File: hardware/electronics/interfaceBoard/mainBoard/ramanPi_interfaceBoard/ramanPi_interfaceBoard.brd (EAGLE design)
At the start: 151.1 x 89.8 mm, 11 parts

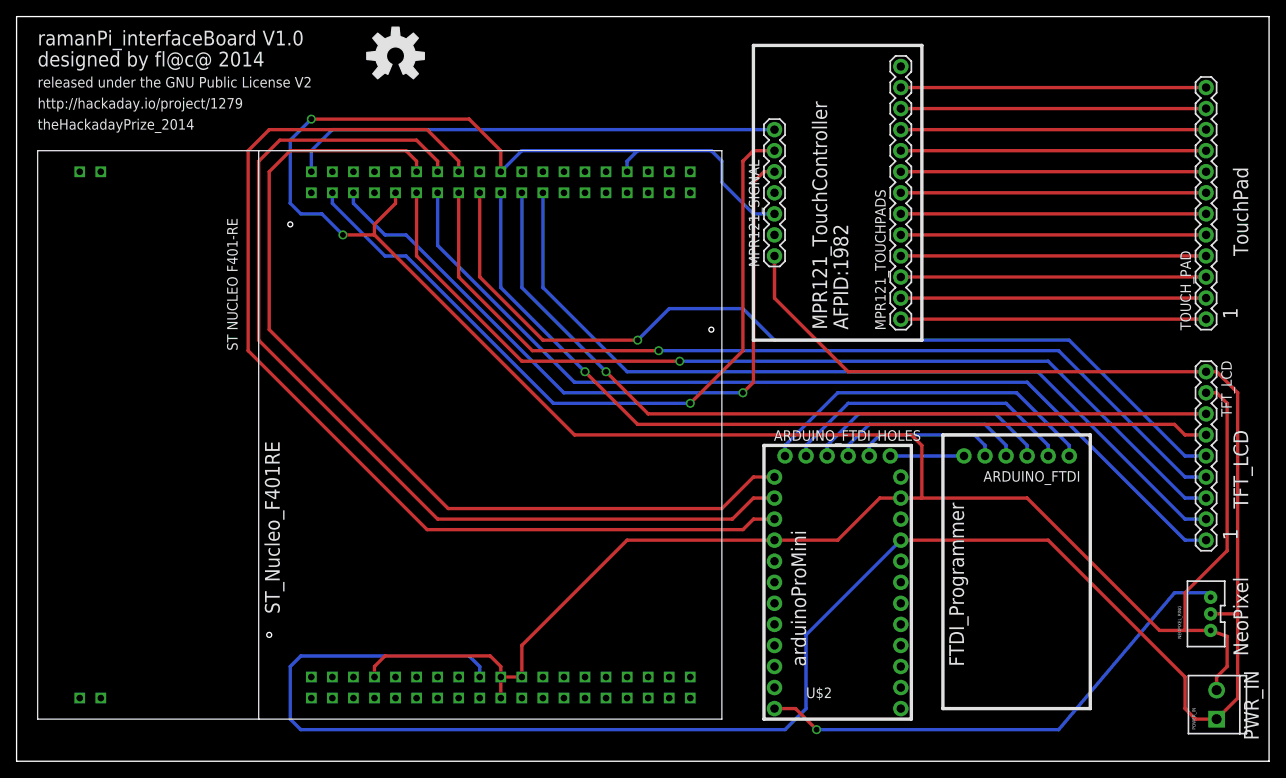
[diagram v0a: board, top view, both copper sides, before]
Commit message: updated Nucleo library in all board layouts
Updated Nucleo F401_RE library for better drill hole sizes
updated all boards to include new library changes
---need to update all studio files, svg, etc..
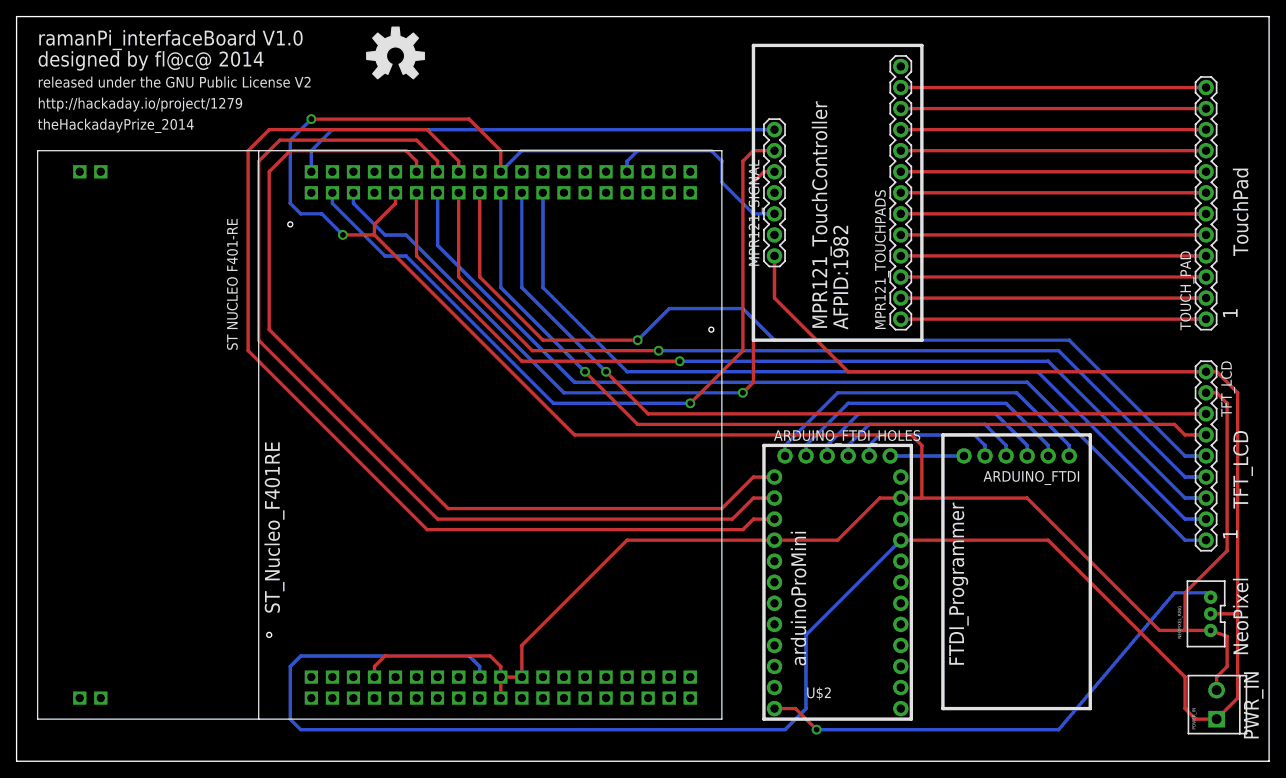
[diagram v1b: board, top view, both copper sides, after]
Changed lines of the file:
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@@
 </classes>
 <designrules>
-<description language="de">&lt;b&gt;EAGLE Design Rules&lt;/b&gt;
-&lt;p&gt;
-Die Standard-Design-Rules sind so gewählt, dass sie für
-die meisten Anwendungen passen. Sollte ihre Platine
-besondere Anforderungen haben, treffen Sie die erforderlichen
-Einstellungen hier und speichern die Design Rules unter
-einem neuen Namen ab.</description>
 <description language="en">&lt;b&gt;EAGLE Design Rules&lt;/b&gt;
 &lt;p&gt;
@@
 <param name="mdViaViaSameLayer" value="8mil"/>
 <param name="mnLayersViaInSmd" value="2"/>
-<param name="mdCopperDimension" value="40mil"/>
+<param name="mdCopperDimension" value="10mil"/>
 <param name="mdDrill" value="8mil"/>
 <param name="mdSmdStop" value="0mil"/>
-<param name="msWidth" value="10mil"/>
-<param name="msDrill" value="24mil"/>
+<param name="msWidth" value="8mil"/>
+<param name="msDrill" value="20mil"/>
 <param name="msMicroVia" value="9.99mm"/>
 <param name="msBlindViaRatio" value="0.5"/>
@@
 <param name="rvMicroViaOuter" value="0.25"/>
 <param name="rvMicroViaInner" value="0.25"/>
-<param name="rlMinPadTop" value="10mil"/>
+<param name="rlMinPadTop" value="12mil"/>
 <param name="rlMaxPadTop" value="20mil"/>
 <param name="rlMinPadInner" value="10mil"/>
 <param name="rlMaxPadInner" value="20mil"/>
-<param name="rlMinPadBottom" value="10mil"/>
+<param name="rlMinPadBottom" value="12mil"/>
 <param name="rlMaxPadBottom" value="20mil"/>
-<param name="rlMinViaOuter" value="8mil"/>
+<param name="rlMinViaOuter" value="10mil"/>
 <param name="rlMaxViaOuter" value="20mil"/>
-<param name="rlMinViaInner" value="8mil"/>
+<param name="rlMinViaInner" value="10mil"/>
 <param name="rlMaxViaInner" value="20mil"/>
 <param name="rlMinMicroViaOuter" value="4mil"/>
@@
 <param name="mlMinCreamFrame" value="0mil"/>
 <param name="mlMaxCreamFrame" value="0mil"/>
-<param name="mlViaStopLimit" value="0mil"/>
+<param name="mlViaStopLimit" value="25mil"/>
 <param name="srRoundness" value="0"/>
 <param name="srMinRoundness" value="0mil"/>

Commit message: update
updated all boards and schematics
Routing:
- net N$25: track 347.2 -> 346.4 mm
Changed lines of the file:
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@@
 <wire x1="146.05" y1="25.4" x2="140.97" y2="20.32" width="0.4064" layer="1"/>
 <wire x1="140.97" y1="20.32" x2="140.97" y2="15.78" width="0.4064" layer="1"/>
-<wire x1="144.78" y1="8.58" x2="144.78" y2="10.16" width="0.4064" layer="1"/>
-<wire x1="144.78" y1="10.16" x2="146.05" y2="11.43" width="0.4064" layer="1"/>
-<wire x1="146.05" y1="11.43" x2="146.05" y2="15.06" width="0.4064" layer="1"/>
-<wire x1="146.05" y1="15.06" x2="144.06" y2="15.78" width="0.4064" layer="1"/>
+<wire x1="144.78" y1="8.58" x2="144.78" y2="15.06" width="0.4064" layer="1"/>
+<wire x1="144.78" y1="15.06" x2="144.06" y2="15.78" width="0.4064" layer="1"/>
 <wire x1="106.68" y1="31.75" x2="104.14" y2="31.75" width="0.4064" layer="1"/>
 <wire x1="104.14" y1="31.75" x2="99.06" y2="26.67" width="0.4064" layer="1"/>
@@
 <wire x1="74.93" y1="73.66" x2="73.66" y2="72.39" width="0.4064" layer="16"/>
 <wire x1="73.66" y1="72.39" x2="73.66" y2="71.12" width="0.4064" layer="16"/>
-<wire x1="58.42" y1="71.12" x2="60.96" y2="73.66" width="0.4064" layer="16"/>
-<wire x1="60.96" y1="73.66" x2="74.93" y2="73.66" width="0.4064" layer="16"/>
+<wire x1="59.69" y1="73.66" x2="74.93" y2="73.66" width="0.4064" layer="16"/>
 <wire x1="58.42" y1="71.12" x2="58.42" y2="73.66" width="0.4064" layer="1"/>
 <wire x1="58.42" y1="73.66" x2="54.61" y2="77.47" width="0.4064" layer="1"/>
@@
 <wire x1="43.18" y1="64.77" x2="45.72" y2="67.31" width="0.4064" layer="1"/>
 <wire x1="45.72" y1="67.31" x2="45.72" y2="68.58" width="0.4064" layer="1"/>
+<wire x1="59.69" y1="73.66" x2="58.42" y2="72.39" width="0.4064" layer="16"/>
+<wire x1="58.42" y1="72.39" x2="58.42" y2="71.12" width="0.4064" layer="16"/>
 </signal>
 <signal name="N$24">

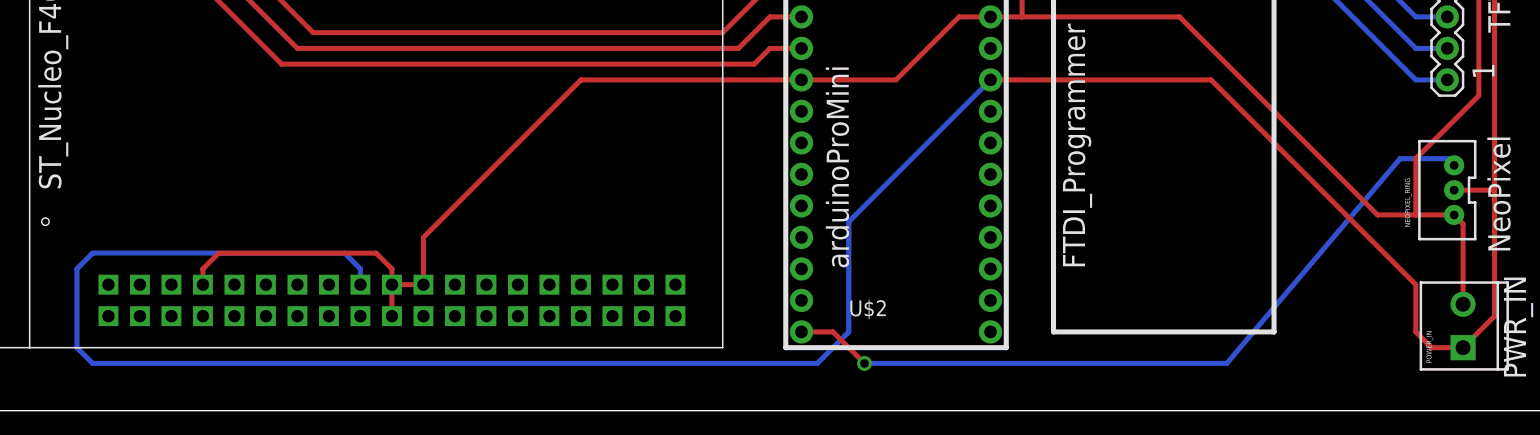
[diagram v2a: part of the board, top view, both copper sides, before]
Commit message: added reset circuitry to all stm32 boards
added reset circuitry for raspi to reset each board from remote.
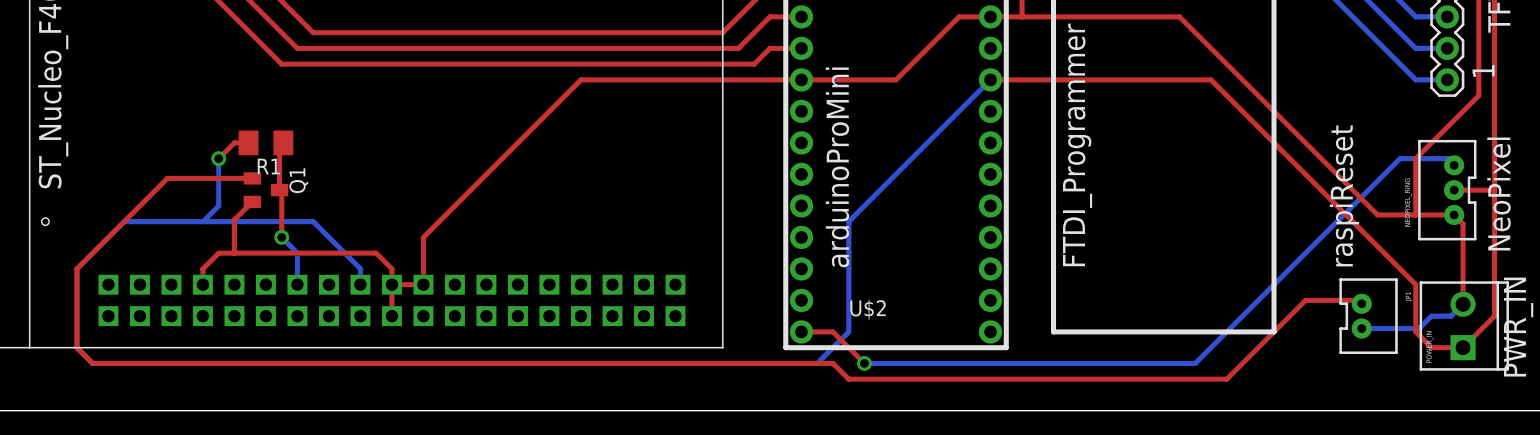
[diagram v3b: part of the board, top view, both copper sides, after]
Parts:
- added JP1: M02JST-PTH-VERT, SparkFun-Connectors:JST-2-PTH-VERT
- added Q1: 2n2222, semicon-smd-ipc:SOT23
- added R1: 10k, adafruit:M1206
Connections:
- removed net N$1: MPR121_SIGNAL.1, NEOPIXEL_RING.2, POWER_IN.1, TFT_LCD.1, U$1.+5V, U$2.21
- removed net N$25: MPR121_SIGNAL.3, NEOPIXEL_RING.1, POWER_IN.2, TFT_LCD.2, U$1.AGND, U$1.GND, U$1.GND2, U$1.GND3, U$1.GND4, U$1.GND5, U$1.GND6, U$2.23, U$2.4
- new net +5V: MPR121_SIGNAL.1, NEOPIXEL_RING.2, POWER_IN.1, R1.2, TFT_LCD.1, U$1.+5V, U$2.21
- new net GND: JP1.2, MPR121_SIGNAL.3, NEOPIXEL_RING.1, POWER_IN.2, Q1.2, TFT_LCD.2, U$1.AGND, U$1.GND, U$1.GND2, U$1.GND3, U$1.GND4, U$1.GND5, U$1.GND6, U$2.23, U$2.4
- new net N$35: Q1.3, R1.1, U$1.NRST
- new net N$36: JP1.1, Q1.1
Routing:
- net GND: track 0.00 -> 360.1 mm, vias 0 -> 2
- net N$25: track 346.4 -> 0.00 mm, vias 2 -> 0
- net +5V: track 0.00 -> 289.7 mm, vias 0 -> 1
- net N$1: track 279.0 -> 0.00 mm
- net N$36: track 0.00 -> 130.9 mm
- net N$35: track 0.00 -> 12.2 mm, vias 0 -> 1
- net N$14: track 61.6 -> 60.7 mm
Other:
- board text added: "raspiReset"
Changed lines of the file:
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@@
 <layer number="21" name="tPlace" color="7" fill="1" visible="yes" active="yes"/>
 <layer number="22" name="bPlace" color="7" fill="1" visible="yes" active="yes"/>
-<layer number="23" name="tOrigins" color="15" fill="1" visible="no" active="yes"/>
-<layer number="24" name="bOrigins" color="15" fill="1" visible="no" active="yes"/>
+<layer number="23" name="tOrigins" color="15" fill="1" visible="yes" active="yes"/>
+<layer number="24" name="bOrigins" color="15" fill="1" visible="yes" active="yes"/>
 <layer number="25" name="tNames" color="7" fill="1" visible="no" active="yes"/>
 <layer number="26" name="bNames" color="7" fill="1" visible="no" active="yes"/>
@@
 <wire x1="90.17" y1="5.08" x2="107.95" y2="5.08" width="0.4064" layer="21"/>
 <wire x1="107.95" y1="5.08" x2="107.95" y2="38.1" width="0.4064" layer="21"/>
+<text x="135.89" y="11.43" size="1.778" layer="21" rot="R90">raspiReset</text>
 </plain>
 <attributes>
@@
 <element name="POWER_IN" library="SparkFun-Connectors" package="SCREWTERMINAL-3.5MM-2" value="M023.5MM" x="144.78" y="5.08" rot="R90"/>
 <element name="U$3" library="SparkFun-Aesthetics" package="OSHW-LOGO-L" value="" x="45.72" y="85.09"/>
+<element name="JP1" library="SparkFun-Connectors" package="JST-2-PTH-VERT" value="M02JST-PTH-VERT" x="137.16" y="7.62" rot="R270"/>
+<element name="Q1" library="semicon-smd-ipc" package="SOT23" value="2n2222" x="48.26" y="17.78" rot="R270"/>
+<element name="R1" library="adafruit" package="M1206" value="10k" x="48.26" y="21.59" rot="R180"/>
 </elements>
 <signals>
@@
 <wire x1="106.68" y1="81.28" x2="143.51" y2="81.28" width="0.4064" layer="1"/>
 </signal>
-<signal name="N$1">
+<signal name="+5V">
 <contactref element="U$1" pad="+5V"/>
 <contactref element="MPR121_SIGNAL" pad="1"/>
@@
 <wire x1="34.29" y1="3.81" x2="33.02" y2="5.08" width="0.4064" layer="16"/>
 <wire x1="33.02" y1="5.08" x2="33.02" y2="11.43" width="0.4064" layer="16"/>
-<wire x1="33.02" y1="11.43" x2="34.29" y2="12.7" width="0.4064" layer="16"/>
-<wire x1="34.29" y1="12.7" x2="54.61" y2="12.7" width="0.4064" layer="16"/>
-<wire x1="54.61" y1="12.7" x2="55.88" y2="11.43" width="0.4064" layer="16"/>
+<wire x1="33.02" y1="11.43" x2="36.83" y2="15.24" width="0.4064" layer="16"/>
+<wire x1="36.83" y1="15.24" x2="43.18" y2="15.24" width="0.4064" layer="16"/>
+<wire x1="43.18" y1="15.24" x2="52.07" y2="15.24" width="0.4064" layer="16"/>
+<wire x1="52.07" y1="15.24" x2="55.88" y2="11.43" width="0.4064" layer="16"/>
 <wire x1="55.88" y1="11.43" x2="55.88" y2="10.16" width="0.4064" layer="16"/>
+<contactref element="R1" pad="2"/>
+<wire x1="46.86" y1="21.59" x2="45.72" y2="21.59" width="0.4064" layer="1"/>
+<wire x1="45.72" y1="21.59" x2="44.45" y2="20.32" width="0.4064" layer="1"/>
+<via x="44.45" y="20.32" extent="1-16" drill="0.7"/>
+<wire x1="44.45" y1="20.32" x2="44.45" y2="16.51" width="0.4064" layer="16"/>
+<wire x1="44.45" y1="16.51" x2="43.18" y2="15.24" width="0.4064" layer="16"/>
 </signal>
 <signal name="N$15">
@@
 <wire x1="144.06" y1="19.78" x2="143.52" y2="20.32" width="0.4064" layer="16"/>
 <wire x1="143.52" y1="20.32" x2="139.7" y2="20.32" width="0.4064" layer="16"/>
-<wire x1="139.7" y1="20.32" x2="125.73" y2="3.81" width="0.4064" layer="16"/>
-<wire x1="125.73" y1="3.81" x2="96.52" y2="3.81" width="0.4064" layer="16"/>
+<wire x1="139.7" y1="20.32" x2="123.19" y2="3.81" width="0.4064" layer="16"/>
+<wire x1="123.19" y1="3.81" x2="96.52" y2="3.81" width="0.4064" layer="16"/>
 <via x="96.52" y="3.81" extent="1-16" drill="0.7"/>
 <wire x1="96.52" y1="3.81" x2="93.98" y2="6.35" width="0.4064" layer="1"/>
 <wire x1="93.98" y1="6.35" x2="91.44" y2="6.35" width="0.4064" layer="1"/>
 </signal>
-<signal name="N$25">
+<signal name="GND">
 <contactref element="NEOPIXEL_RING" pad="1"/>
 <contactref element="U$1" pad="GND6"/>
@@
 <wire x1="58.42" y1="10.16" x2="58.42" y2="7.62" width="0.4064" layer="1"/>
 <wire x1="60.96" y1="10.16" x2="58.42" y2="10.16" width="0.4064" layer="1"/>
-<wire x1="43.18" y1="10.16" x2="43.18" y2="11.43" width="0.4064" layer="1"/>
-<wire x1="43.18" y1="11.43" x2="44.45" y2="12.7" width="0.4064" layer="1"/>
-<wire x1="44.45" y1="12.7" x2="57.15" y2="12.7" width="0.4064" layer="1"/>
+<wire x1="45.72" y1="12.7" x2="57.15" y2="12.7" width="0.4064" layer="1"/>
 <wire x1="57.15" y1="12.7" x2="58.42" y2="11.43" width="0.4064" layer="1"/>
 <wire x1="58.42" y1="11.43" x2="58.42" y2="10.16" width="0.4064" layer="1"/>
@@
 <wire x1="59.69" y1="73.66" x2="58.42" y2="72.39" width="0.4064" layer="16"/>
 <wire x1="58.42" y1="72.39" x2="58.42" y2="71.12" width="0.4064" layer="16"/>
+<contactref element="JP1" pad="2"/>
+<contactref element="Q1" pad="2"/>
+<wire x1="43.18" y1="10.16" x2="43.18" y2="11.43" width="0.4064" layer="1"/>
+<wire x1="43.18" y1="11.43" x2="44.45" y2="12.7" width="0.4064" layer="1"/>
+<wire x1="44.45" y1="12.7" x2="45.72" y2="12.7" width="0.4064" layer="1"/>
+<wire x1="45.72" y1="12.7" x2="45.72" y2="15.39" width="0.4064" layer="1"/>
+<wire x1="45.72" y1="15.39" x2="47.16" y2="16.83" width="0.4064" layer="1"/>
+<wire x1="136.61" y1="6.62" x2="141.24" y2="6.62" width="0.4064" layer="16"/>
+<wire x1="141.24" y1="6.62" x2="142.24" y2="7.62" width="0.4064" layer="16"/>
+<wire x1="142.24" y1="7.62" x2="143.82" y2="7.62" width="0.4064" layer="16"/>
+<wire x1="143.82" y1="7.62" x2="144.78" y2="8.58" width="0.4064" layer="16"/>
 </signal>
 <signal name="N$24">
@@
 <wire x1="50.8" y1="62.23" x2="50.8" y2="68.58" width="0.4064" layer="16"/>
 </signal>
+<signal name="N$35">
+<contactref element="U$1" pad="NRST"/>
+<contactref element="Q1" pad="3"/>
+<contactref element="R1" pad="1"/>
+<wire x1="50.8" y1="10.16" x2="50.8" y2="12.7" width="0.4064" layer="16"/>
+<wire x1="50.8" y1="12.7" x2="49.53" y2="13.97" width="0.4064" layer="16"/>
+<via x="49.53" y="13.97" extent="1-16" drill="0.7"/>
+<wire x1="49.53" y1="13.97" x2="49.53" y2="17.61" width="0.4064" layer="1"/>
+<wire x1="49.53" y1="17.61" x2="49.36" y2="17.78" width="0.4064" layer="1"/>
+<wire x1="49.36" y1="17.78" x2="49.36" y2="21.29" width="0.4064" layer="1"/>
+<wire x1="49.36" y1="21.29" x2="49.66" y2="21.59" width="0.4064" layer="1"/>
+</signal>
+<signal name="N$36">
+<contactref element="JP1" pad="1"/>
+<contactref element="Q1" pad="1"/>
+<wire x1="47.16" y1="18.73" x2="40.32" y2="18.73" width="0.4064" layer="1"/>
+<wire x1="40.32" y1="18.73" x2="33.02" y2="11.43" width="0.4064" layer="1"/>
+<wire x1="33.02" y1="11.43" x2="33.02" y2="5.08" width="0.4064" layer="1"/>
+<wire x1="33.02" y1="5.08" x2="34.29" y2="3.81" width="0.4064" layer="1"/>
+<wire x1="34.29" y1="3.81" x2="93.98" y2="3.81" width="0.4064" layer="1"/>
+<wire x1="93.98" y1="3.81" x2="95.25" y2="2.54" width="0.4064" layer="1"/>
+<wire x1="95.25" y1="2.54" x2="125.73" y2="2.54" width="0.4064" layer="1"/>
+<wire x1="125.73" y1="2.54" x2="132.08" y2="8.89" width="0.4064" layer="1"/>
+<wire x1="132.08" y1="8.89" x2="136.34" y2="8.89" width="0.4064" layer="1"/>
+<wire x1="136.34" y1="8.89" x2="136.61" y2="8.62" width="0.4064" layer="1"/>
+</signal>
 </signals>
